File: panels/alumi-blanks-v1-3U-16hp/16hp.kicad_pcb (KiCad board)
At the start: 2 copper layers, 80.9 x 128.5 mm, 2 parts

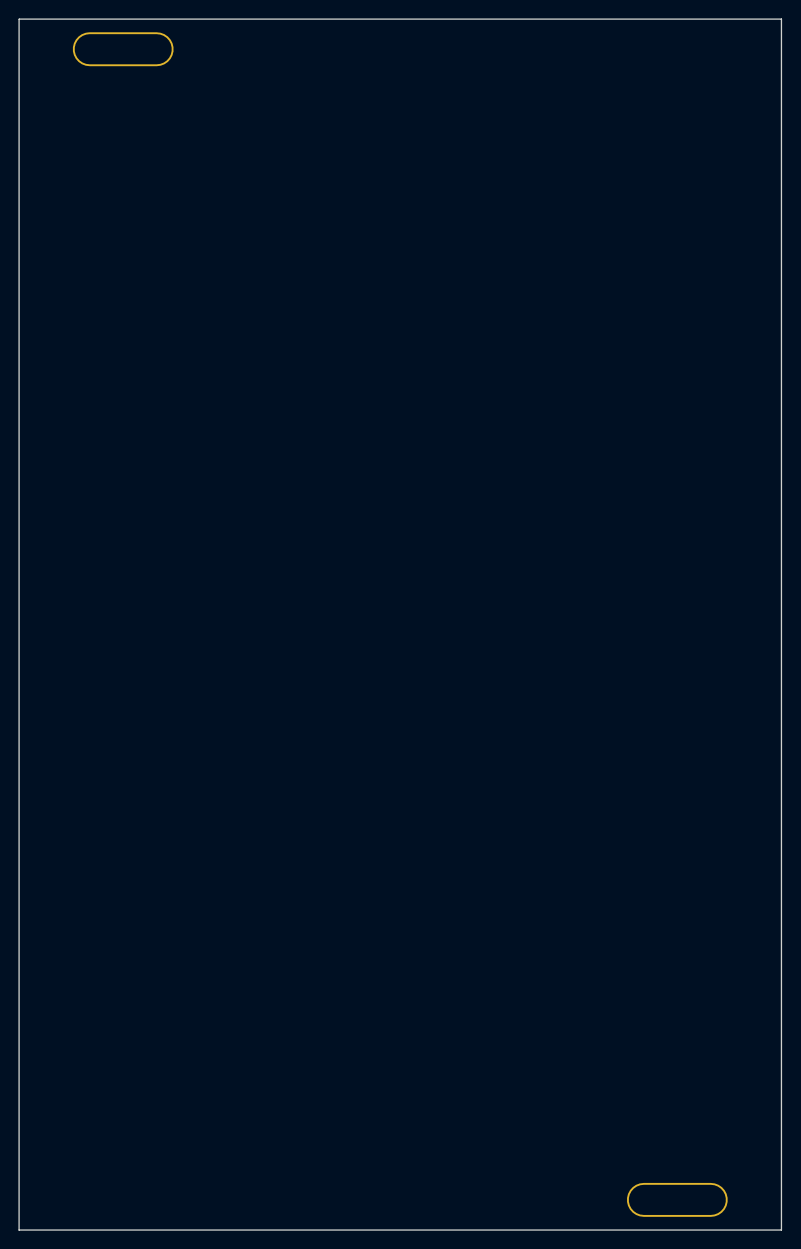
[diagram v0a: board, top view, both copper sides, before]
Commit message: feat: add new screw hole footprints and update panel KiCad files for new JLCPCB order
- Added modular-3M-screw-hole-size1-alumi-0604, modular-3M-screw-hole-size1-fit-alumi-0604, modular-3M-screw-hole-size2-alumi-0604
- Updated all panel .kicad_pcb and .kicad_pro files for 3U panels (1hp-16hp)
- Added new JLCPCB order snapshot and Gerber outputs

Co-authored-by: Copilot <223556219+Copilot@users.noreply.github.com>
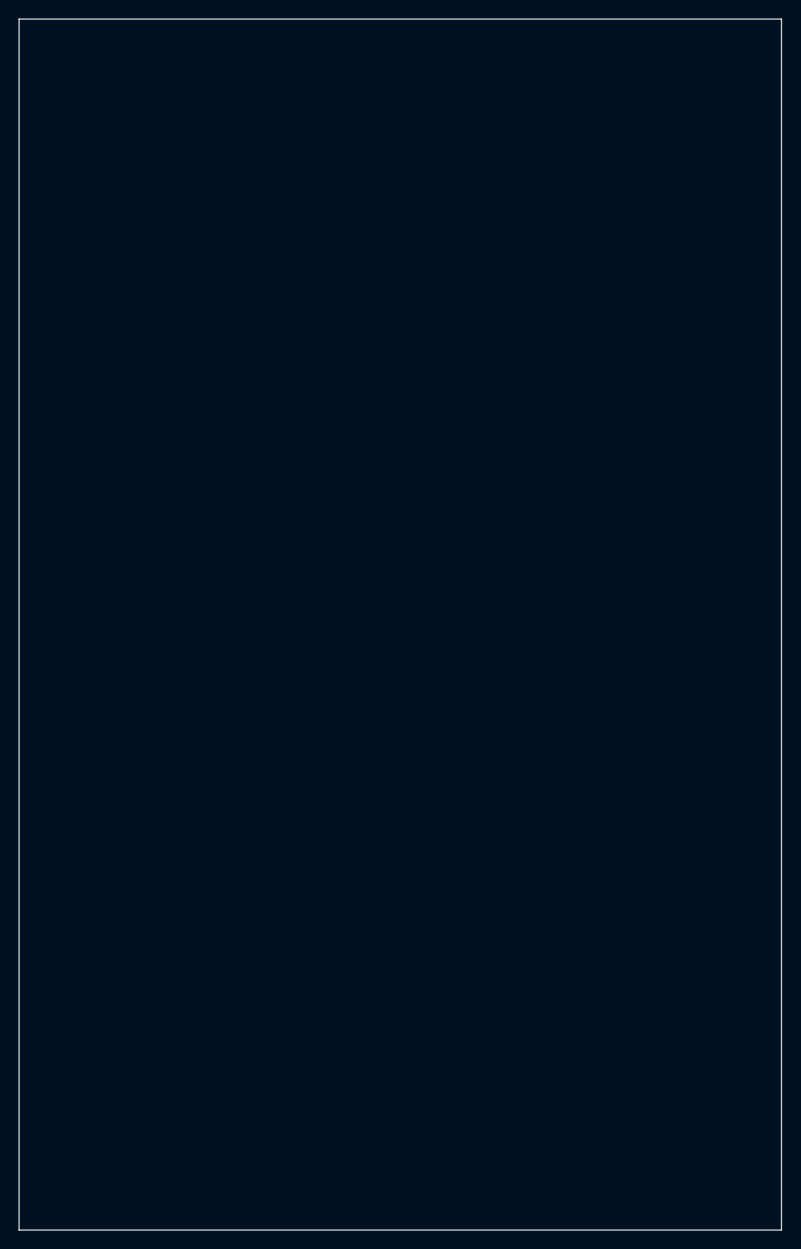
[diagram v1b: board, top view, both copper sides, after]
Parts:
- removed the REF** at (11.1, 3.20)
- removed the REF** at (69.8, 125.3)
- added REF**: modular-3M-screw-hole-size2-alumi-0604, zudo-blanks:modular-3M-screw-hole-size2-alumi-0604, F.Cu at (70.7, 125.5)
- added REF**: modular-3M-screw-hole-size2-alumi-0604, zudo-blanks:modular-3M-screw-hole-size2-alumi-0604, F.Cu at (10.2, 125.5)
- added REF**: modular-3M-screw-hole-size2-alumi-0604, zudo-blanks:modular-3M-screw-hole-size2-alumi-0604, F.Cu at (10.2, 3.00)
- added REF**: modular-3M-screw-hole-size2-alumi-0604, zudo-blanks:modular-3M-screw-hole-size2-alumi-0604, F.Cu at (70.7, 3.00)
